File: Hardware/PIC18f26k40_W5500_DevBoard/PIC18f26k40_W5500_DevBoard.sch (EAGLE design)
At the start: 59 parts, among them J2 MAGJACK, J6 USB-B, U1 W5500, U2 PIC18F2523-I/SO, Y2 CRYSTAL-GROUNDEDSMD-3.2X2.5

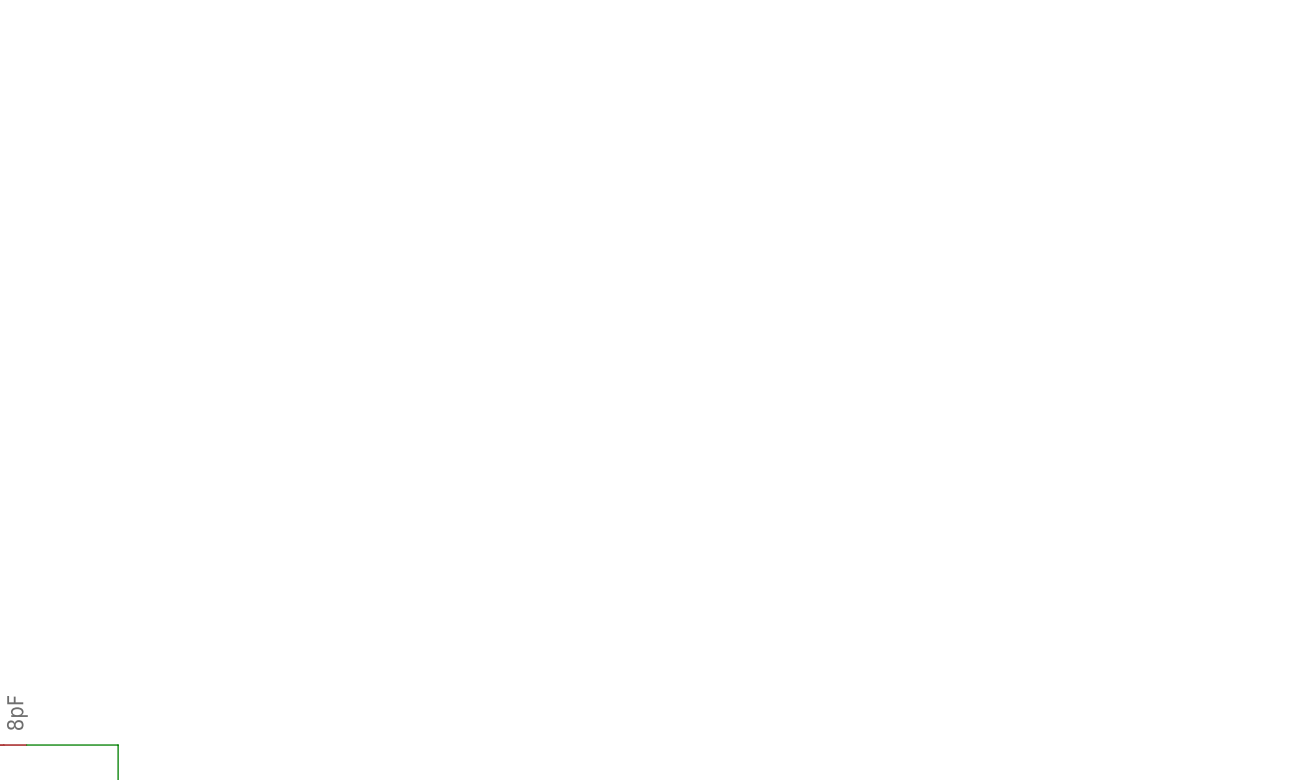
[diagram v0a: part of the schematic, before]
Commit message: #302 Added AC Playground to dev board
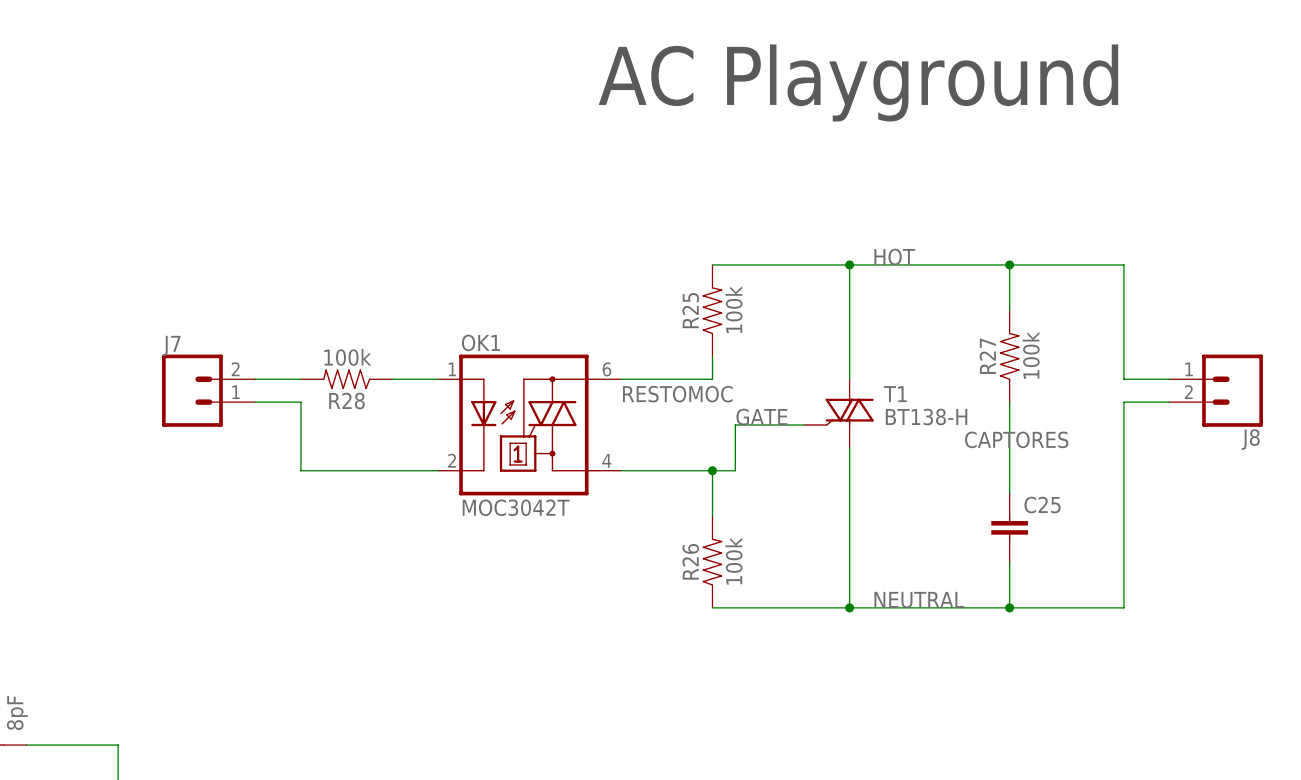
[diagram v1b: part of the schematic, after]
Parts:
- added C25: (no value), SparkFun-Capacitors:CAPPTH3
- added J7: (no value), SparkFun-Connectors:CONN_02
- added J8: (no value), SparkFun-Connectors:CONN_025MM
- added OK1: MOC3042T, optocoupler:MOC3042T
- added R25, R26, R27, R28: 100k, SparkFun-Resistors:100KOHM-HORIZ-1/4W-1%
- added T1: BT138-H, triac:BT138-H
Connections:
- new net CAPTORES: C25.1, R27.1
- new net GATE: OK1.A1, R26.2, T1.G
- new net HOT: J8.1, R25.2, R27.2, T1.A2
- new net N$18: OK1.A, R28.1
- new net N$19: J7.1, OK1.C
- new net N$5: J7.2, R28.2
- new net NEUTRAL: C25.2, J8.2, R26.1, T1.A1
- new net RESTOMOC: OK1.A2, R25.1
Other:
- note added: "AC Playground"
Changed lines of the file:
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@@
 <part name="GND20" library="SparkFun-Aesthetics" deviceset="GND" device=""/>
 <part name="R24" library="SparkFun-Passives" deviceset="RESISTOR" device="0603-RES" value="1Meg"/>
+<part name="OK1" library="optocoupler" deviceset="MOC30*" device="T" technology="42"/>
+<part name="J8" library="SparkFun-Connectors" deviceset="CONN_02" device="5MM"/>
+<part name="R25" library="SparkFun-Resistors" deviceset="100KOHM" device="-HORIZ-1/4W-1%" value="100k"/>
+<part name="R26" library="SparkFun-Resistors" deviceset="100KOHM" device="-HORIZ-1/4W-1%" value="100k"/>
+<part name="T1" library="triac" deviceset="BT138" device="-H"/>
+<part name="C25" library="SparkFun-Capacitors" deviceset="CAP" device="PTH3"/>
+<part name="R27" library="SparkFun-Resistors" deviceset="100KOHM" device="-HORIZ-1/4W-1%" value="100k"/>
+<part name="R28" library="SparkFun-Resistors" deviceset="100KOHM" device="-HORIZ-1/4W-1%" value="100k"/>
+<part name="J7" library="SparkFun-Connectors" deviceset="CONN_02" device=""/>
 </parts>
 <sheets>
@@
 <text x="294.64" y="53.34" size="2.54" layer="97">W5500 VCCA Filter</text>
 <text x="248.92" y="-30.48" size="5.08" layer="97">MagJack (Magnetics Inside)</text>
+<text x="368.3" y="160.02" size="6.4516" layer="97">AC Playground</text>
 </plain>
 <instances>
@@
 <instance part="GND20" gate="1" x="294.64" y="83.82" rot="R90"/>
 <instance part="R24" gate="G$1" x="276.86" y="83.82" rot="R90"/>
+<instance part="OK1" gate="-1" x="360.68" y="124.46"/>
+<instance part="J8" gate="G$1" x="439.42" y="129.54" rot="R180"/>
+<instance part="R25" gate="G$1" x="381" y="137.16" rot="R90"/>
+<instance part="R26" gate="G$1" x="381" y="109.22" rot="R90"/>
+<instance part="T1" gate="G$1" x="396.24" y="124.46"/>
+<instance part="C25" gate="G$1" x="414.02" y="111.76"/>
+<instance part="R27" gate="G$1" x="414.02" y="132.08" rot="R90"/>
+<instance part="R28" gate="G$1" x="340.36" y="129.54" rot="R180"/>
+<instance part="J7" gate="G$1" x="322.58" y="127"/>
 </instances>
 <busses>
@@
 </segment>
 </net>
+<net name="N$5" class="0">
+<segment>
+<pinref part="J7" gate="G$1" pin="2"/>
+<pinref part="R28" gate="G$1" pin="2"/>
+<wire x1="330.2" y1="129.54" x2="335.28" y2="129.54" width="0.1524" layer="91"/>
+</segment>
+</net>
+<net name="N$18" class="0">
+<segment>
+<pinref part="R28" gate="G$1" pin="1"/>
+<pinref part="OK1" gate="-1" pin="A"/>
+<wire x1="345.44" y1="129.54" x2="350.52" y2="129.54" width="0.1524" layer="91"/>
+</segment>
+</net>
+<net name="N$19" class="0">
+<segment>
+<pinref part="OK1" gate="-1" pin="C"/>
+<wire x1="350.52" y1="119.38" x2="335.28" y2="119.38" width="0.1524" layer="91"/>
+<wire x1="335.28" y1="119.38" x2="335.28" y2="127" width="0.1524" layer="91"/>
+<pinref part="J7" gate="G$1" pin="1"/>
+<wire x1="335.28" y1="127" x2="330.2" y2="127" width="0.1524" layer="91"/>
+</segment>
+</net>
+<net name="GATE" class="0">
+<segment>
+<pinref part="OK1" gate="-1" pin="A1"/>
+<wire x1="370.84" y1="119.38" x2="381" y2="119.38" width="0.1524" layer="91"/>
+<wire x1="381" y1="119.38" x2="383.54" y2="119.38" width="0.1524" layer="91"/>
+<wire x1="383.54" y1="119.38" x2="383.54" y2="124.46" width="0.1524" layer="91"/>
+<pinref part="T1" gate="G$1" pin="G"/>
+<wire x1="383.54" y1="124.46" x2="391.16" y2="124.46" width="0.1524" layer="91"/>
+<pinref part="R26" gate="G$1" pin="2"/>
+<wire x1="381" y1="114.3" x2="381" y2="119.38" width="0.1524" layer="91"/>
+<junction x="381" y="119.38"/>
+<label x="383.54" y="124.46" size="1.778" layer="95"/>
+</segment>
+</net>
+<net name="HOT" class="0">
+<segment>
+<pinref part="T1" gate="G$1" pin="A2"/>
+<wire x1="396.24" y1="129.54" x2="396.24" y2="142.24" width="0.1524" layer="91"/>
+<pinref part="R25" gate="G$1" pin="2"/>
+<wire x1="396.24" y1="142.24" x2="381" y2="142.24" width="0.1524" layer="91"/>
+<pinref part="J8" gate="G$1" pin="1"/>
+<wire x1="431.8" y1="129.54" x2="426.72" y2="129.54" width="0.1524" layer="91"/>
+<wire x1="426.72" y1="129.54" x2="426.72" y2="142.24" width="0.1524" layer="91"/>
+<wire x1="426.72" y1="142.24" x2="414.02" y2="142.24" width="0.1524" layer="91"/>
+<junction x="396.24" y="142.24"/>
+<pinref part="R27" gate="G$1" pin="2"/>
+<wire x1="414.02" y1="142.24" x2="396.24" y2="142.24" width="0.1524" layer="91"/>
+<wire x1="414.02" y1="137.16" x2="414.02" y2="142.24" width="0.1524" layer="91"/>
+<junction x="414.02" y="142.24"/>
+<label x="398.78" y="142.24" size="1.778" layer="95"/>
+</segment>
+</net>
+<net name="RESTOMOC" class="0">
+<segment>
+<pinref part="R25" gate="G$1" pin="1"/>
+<wire x1="381" y1="132.08" x2="381" y2="129.54" width="0.1524" layer="91"/>
+<pinref part="OK1" gate="-1" pin="A2"/>
+<wire x1="381" y1="129.54" x2="370.84" y2="129.54" width="0.1524" layer="91"/>
+<label x="370.84" y="127" size="1.778" layer="95"/>
+</segment>
+</net>
+<net name="NEUTRAL" class="0">
+<segment>
+<pinref part="J8" gate="G$1" pin="2"/>
+<wire x1="431.8" y1="127" x2="426.72" y2="127" width="0.1524" layer="91"/>
+<wire x1="426.72" y1="127" x2="426.72" y2="104.14" width="0.1524" layer="91"/>
+<pinref part="R26" gate="G$1" pin="1"/>
+<wire x1="426.72" y1="104.14" x2="414.02" y2="104.14" width="0.1524" layer="91"/>
+<pinref part="T1" gate="G$1" pin="A1"/>
+<wire x1="414.02" y1="104.14" x2="396.24" y2="104.14" width="0.1524" layer="91"/>
+<wire x1="396.24" y1="104.14" x2="381" y2="104.14" width="0.1524" layer="91"/>
+<wire x1="396.24" y1="121.92" x2="396.24" y2="104.14" width="0.1524" layer="91"/>
+<junction x="396.24" y="104.14"/>
+<pinref part="C25" gate="G$1" pin="2"/>
+<wire x1="414.02" y1="109.22" x2="414.02" y2="104.14" width="0.1524" layer="91"/>
+<junction x="414.02" y="104.14"/>
+<label x="398.78" y="104.14" size="1.778" layer="95"/>
+</segment>
+</net>
+<net name="CAPTORES" class="0">
+<segment>
+<pinref part="C25" gate="G$1" pin="1"/>
+<pinref part="R27" gate="G$1" pin="1"/>
+<wire x1="414.02" y1="116.84" x2="414.02" y2="127" width="0.1524" layer="91"/>
+<label x="408.94" y="121.92" size="1.778" layer="95"/>
+</segment>
+</net>

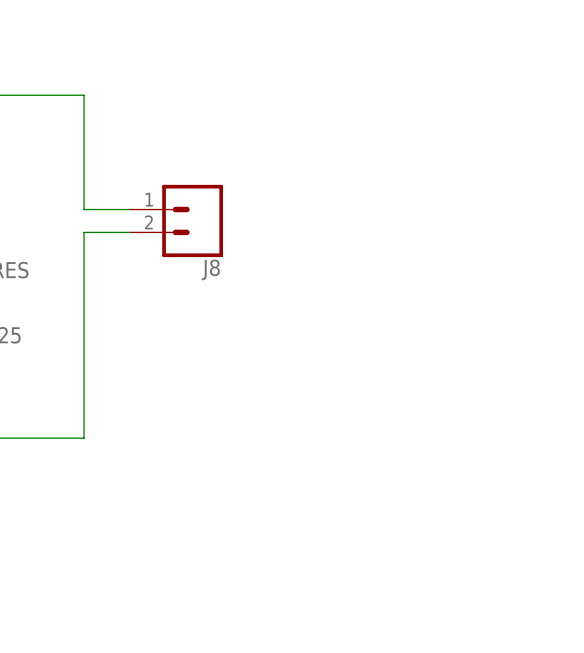
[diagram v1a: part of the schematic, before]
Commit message: #302 Added play zone to AC Playground
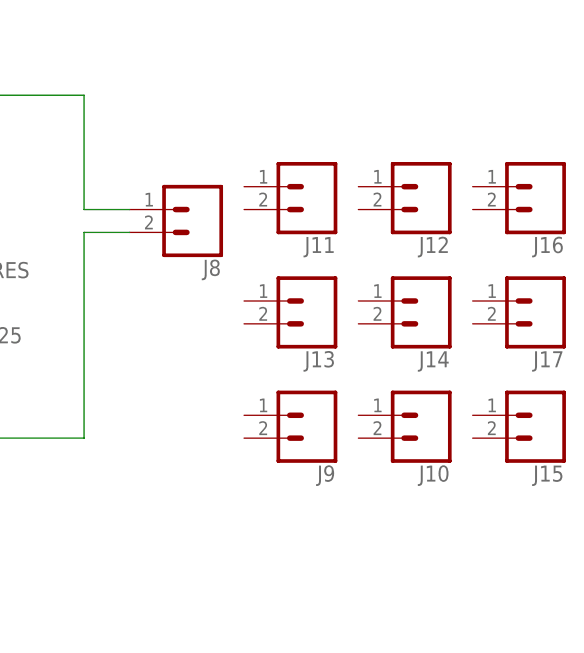
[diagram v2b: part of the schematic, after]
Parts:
- added J10, J11, J12, J13, J14, J15, J16, J17, J9: (no value), SparkFun-Connectors:CONN_025MM
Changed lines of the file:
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@@
 <part name="R28" library="SparkFun-Resistors" deviceset="100KOHM" device="-HORIZ-1/4W-1%" value="100k"/>
 <part name="J7" library="SparkFun-Connectors" deviceset="CONN_02" device=""/>
+<part name="J11" library="SparkFun-Connectors" deviceset="CONN_02" device="5MM"/>
+<part name="J12" library="SparkFun-Connectors" deviceset="CONN_02" device="5MM"/>
+<part name="J13" library="SparkFun-Connectors" deviceset="CONN_02" device="5MM"/>
+<part name="J14" library="SparkFun-Connectors" deviceset="CONN_02" device="5MM"/>
+<part name="J9" library="SparkFun-Connectors" deviceset="CONN_02" device="5MM"/>
+<part name="J10" library="SparkFun-Connectors" deviceset="CONN_02" device="5MM"/>
+<part name="J15" library="SparkFun-Connectors" deviceset="CONN_02" device="5MM"/>
+<part name="J16" library="SparkFun-Connectors" deviceset="CONN_02" device="5MM"/>
+<part name="J17" library="SparkFun-Connectors" deviceset="CONN_02" device="5MM"/>
 </parts>
 <sheets>
@@
 <instance part="R28" gate="G$1" x="340.36" y="129.54" rot="R180"/>
 <instance part="J7" gate="G$1" x="322.58" y="127"/>
+<instance part="J11" gate="G$1" x="452.12" y="132.08" rot="R180"/>
+<instance part="J12" gate="G$1" x="464.82" y="132.08" rot="R180"/>
+<instance part="J13" gate="G$1" x="452.12" y="119.38" rot="R180"/>
+<instance part="J14" gate="G$1" x="464.82" y="119.38" rot="R180"/>
+<instance part="J9" gate="G$1" x="452.12" y="106.68" rot="R180"/>
+<instance part="J10" gate="G$1" x="464.82" y="106.68" rot="R180"/>
+<instance part="J15" gate="G$1" x="477.52" y="106.68" rot="R180"/>
+<instance part="J16" gate="G$1" x="477.52" y="132.08" rot="R180"/>
+<instance part="J17" gate="G$1" x="477.52" y="119.38" rot="R180"/>
 </instances>
 <busses>
